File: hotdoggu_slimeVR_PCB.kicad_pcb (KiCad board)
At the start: 2 copper layers, 18.8 x 88.6 mm, 8 parts, among them J1 Conn_01x04_Pin, J2 Conn_01x02_Pin, SW1 SW_SPDT_312, U2 module_mpu6050

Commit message: pattern, sym, footprint update
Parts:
- U1: footprint hotdoggu_slimeVR_PCB:Geekble_Mini_ESP32C3 -> hotdoggu_slimeVR_PCB:Geekble_Mini_ESP32C3_SMD
- moved SW1 2.97 mm to (153.2, 112.5)
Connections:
- J1 pad 1: GND -> /SDA
- J1 pad 3: /SDA -> /SCL
- J1 pad 4: /SCL -> GND
- R1 pad 2: Net-(U1-D0) -> Net-(U1-GPIO0)
- R2 pad 1: Net-(U1-D0) -> Net-(U1-GPIO0)
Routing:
- net /VBAT_SW: track 58.7 -> 61.7 mm
- net unconnected-(U1-D21/TX-Pad11): track 0.00 -> 2.60 mm, vias 0 -> 1
- net +3V3: track 4.08 -> 1.48 mm, vias 2 -> 1
- net /SDA: track 80.2 -> 78.1 mm, vias 2 -> 1
- net /SCL: track 77.6 -> 76.1 mm
- net +BATT: track 13.5 -> 12.3 mm

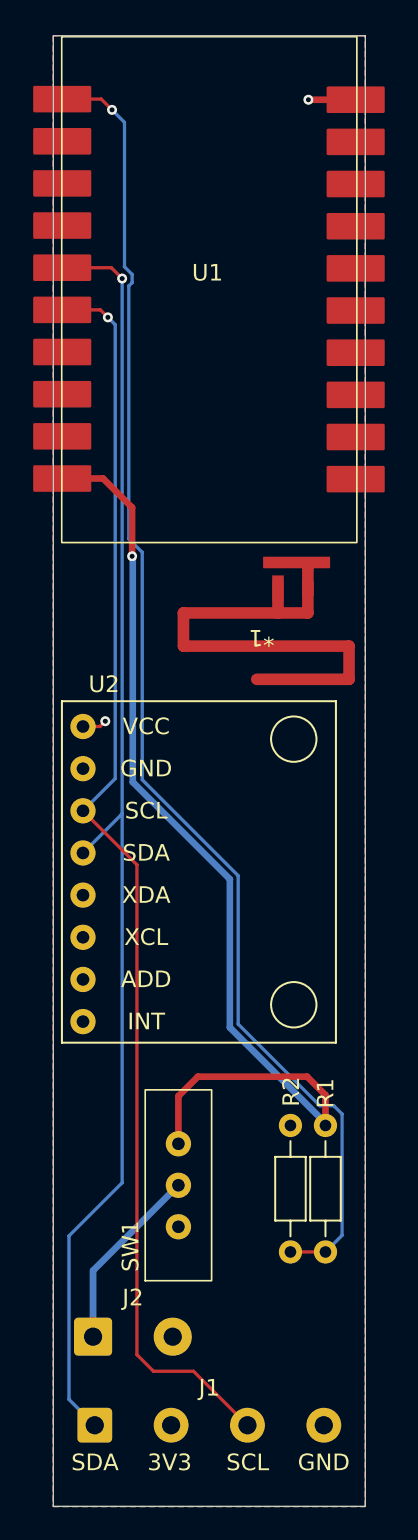
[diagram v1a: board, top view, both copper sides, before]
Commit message: seperate sym, lib / update routing
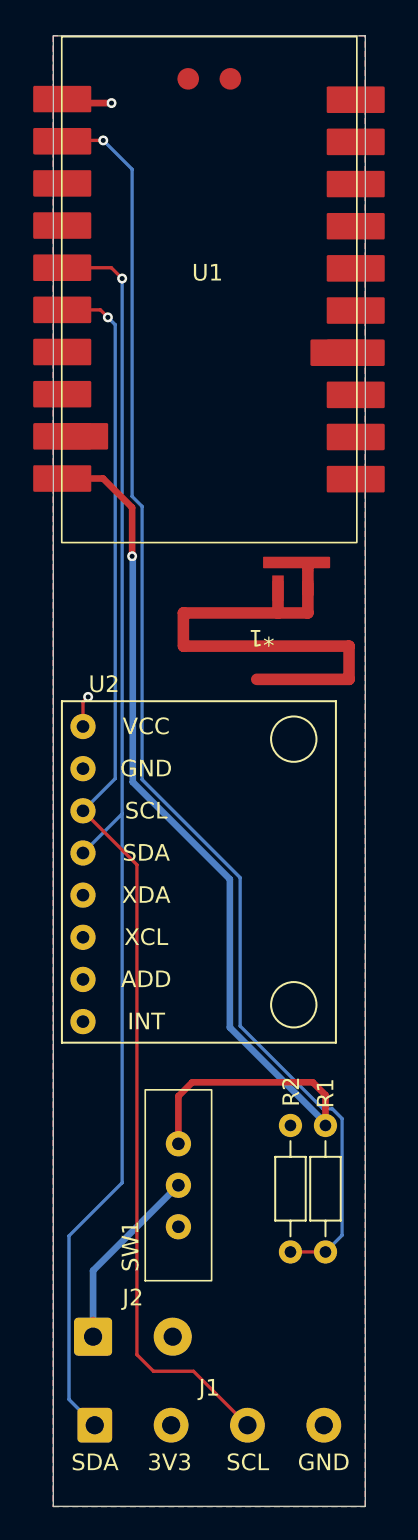
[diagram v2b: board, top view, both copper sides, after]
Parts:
- U1: footprint hotdoggu_slimeVR_PCB:Geekble_Mini_ESP32C3_SMD -> Geekble Mini ESP32C3FH4:Geekble_Mini_ESP32C3FH4_V2.0_SMD
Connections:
- R1 pad 2: Net-(U1-GPIO0) -> Net-(U1-GPIO0/A0)
- R2 pad 1: Net-(U1-GPIO0) -> Net-(U1-GPIO0/A0)
- U1 pad 1: /VBAT_SW -> +3V3
- U1 pad 10: Net-(U1-D0) -> /VBAT_SW
- U1 pad 14: GND -> unconnected-(U1-GPIO7/D7-Pad14)
- U1 pad 17: unconnected-(U1-D8-Pad17) -> GND
- U1 pad 2: GND -> Net-(U1-GPIO0/A0)
- U1 pad 20: +3V3 -> unconnected-(U1-GPIO21/TX-Pad20)
- U1 pad 5: /SCL -> /SDA
- U1 pad 6: /SDA -> /SCL
- U1 pad 9: unconnected-(U1-D1-Pad9) -> GND
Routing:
- net Net-(U1-D0): track 80.8 -> 0.00 mm, vias 1 -> 0
- net Net-(U1-GPIO0/A0): track 0.00 -> 78.2 mm, vias 0 -> 1
- net +3V3: track 1.48 -> 4.91 mm, vias 1 -> 2
- net unconnected-(U1-GPIO10/D10-Pad11): track 2.60 -> 0.00 mm, vias 1 -> 0
